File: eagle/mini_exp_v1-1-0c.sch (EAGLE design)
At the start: 34 parts, among them J1 CR22A-44D-2.54DS(70)STRAIGHT, J2 CR22A-44D-2.54DS(70)STRAIGHT, J3 DB9-MALE-RA, J4 DB9-MALE-RA, Q1 2N3904, U1 AY-3-8910, U2 74LS244N, U3 74LS244N, U4 74LS74N, U5 74LS30N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

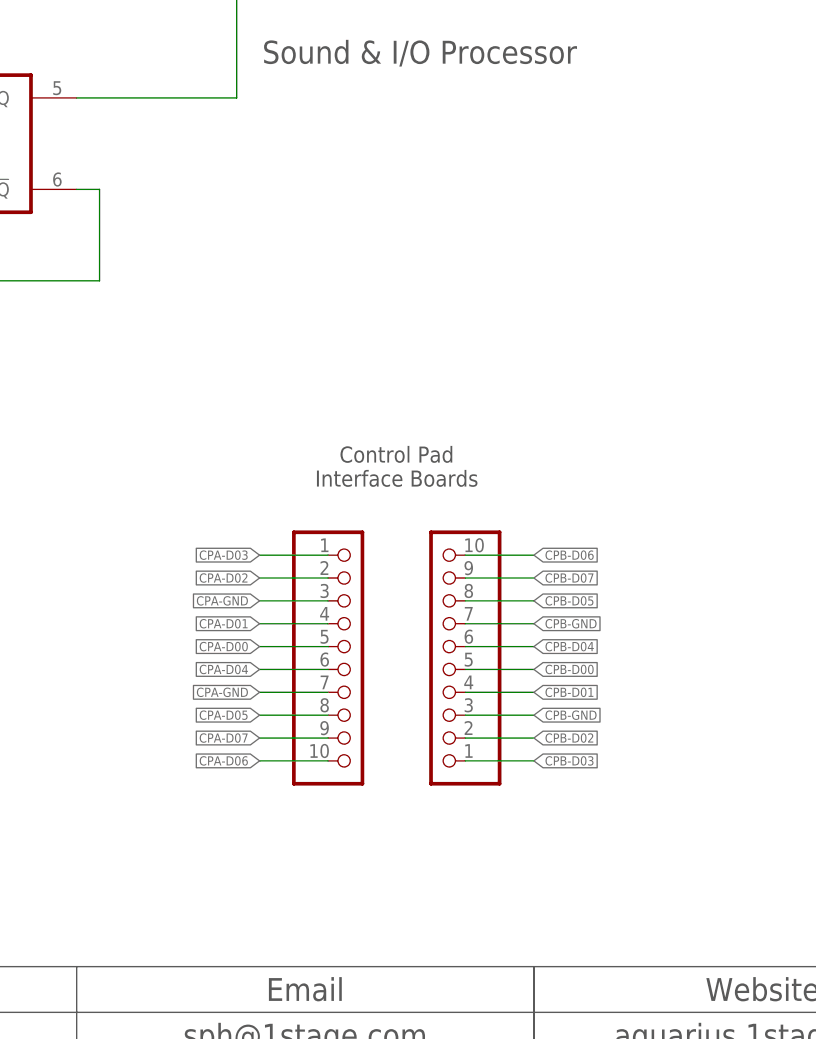
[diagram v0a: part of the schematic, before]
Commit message: Added IO Header to Rev C
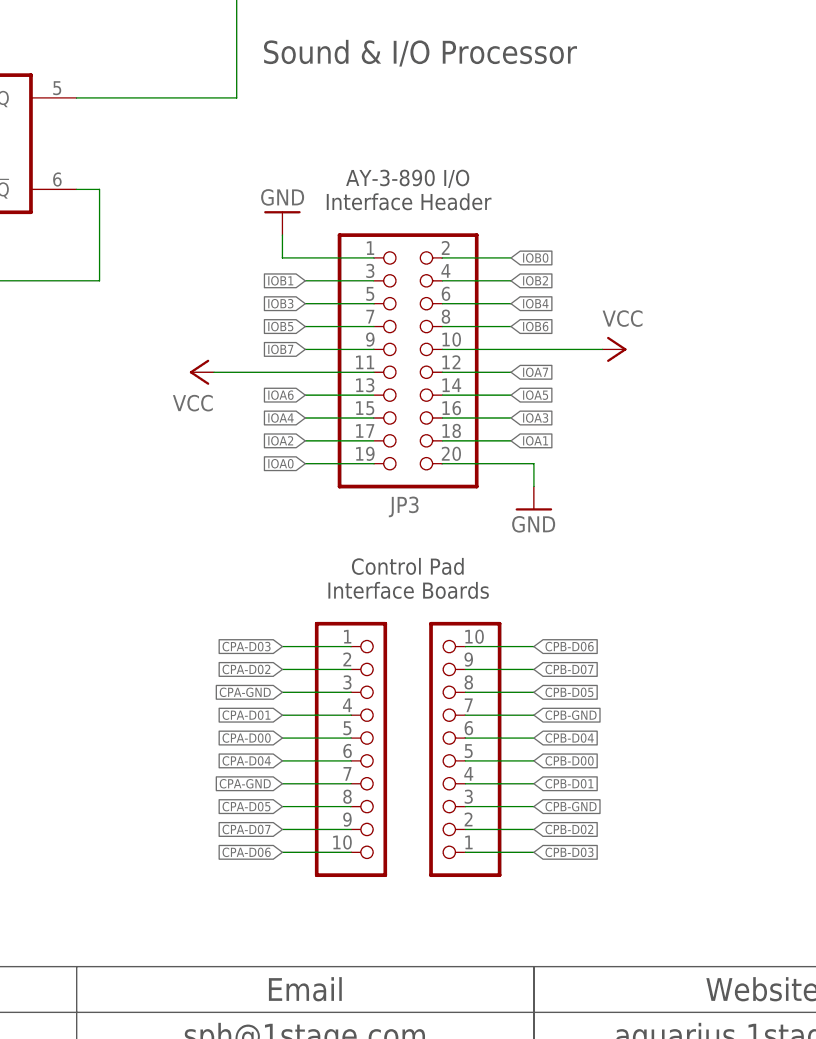
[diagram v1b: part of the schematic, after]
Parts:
- added JP3: (no value), aquarius2:PINHD-2X10
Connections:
- removed net N$100: J4.P$3, U1.IOB6
- removed net N$101: J4.P$9, U1.IOB3
- removed net N$102: J3.P$2, U1.IOA7
- removed net N$103: J3.P$3, U1.IOA6
- removed net N$104: J3.P$4, U1.IOA5
- removed net N$105: J3.P$5, U1.IOA4
- removed net N$106: J3.P$6, U1.IOA0
- removed net N$107: J3.P$7, U1.IOA1
- removed net N$108: J3.P$8, U1.IOA2
- removed net N$109: J3.P$9, U1.IOA3
- removed net N$18: J4.P$6, U1.IOB0
- removed net N$94: J4.P$2, U1.IOB7
- removed net N$95: J4.P$7, U1.IOB1
- removed net N$96: J4.P$8, U1.IOB2
- removed net N$98: J4.P$5, U1.IOB4
- removed net N$99: J4.P$4, U1.IOB5
- new net IOA0: J3.P$6, JP3.19, U1.IOA0
- new net IOA1: J3.P$7, JP3.18, U1.IOA1
- new net IOA2: J3.P$8, JP3.17, U1.IOA2
- new net IOA3: J3.P$9, JP3.16, U1.IOA3
- new net IOA4: J3.P$5, JP3.15, U1.IOA4
- new net IOA5: J3.P$4, JP3.14, U1.IOA5
- new net IOA6: J3.P$3, JP3.13, U1.IOA6
- new net IOA7: J3.P$2, JP3.12, U1.IOA7
- new net IOB0: J4.P$6, JP3.2, U1.IOB0
- new net IOB1: J4.P$7, JP3.3, U1.IOB1
- new net IOB2: J4.P$8, JP3.4, U1.IOB2
- new net IOB3: J4.P$9, JP3.5, U1.IOB3
- new net IOB4: J4.P$5, JP3.6, U1.IOB4
- new net IOB5: J4.P$4, JP3.7, U1.IOB5
- new net IOB6: J4.P$3, JP3.8, U1.IOB6
- new net IOB7: J4.P$2, JP3.9, U1.IOB7
- net GND: now also JP3.1, JP3.20
- net VCC: now also JP3.10, JP3.11
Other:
- note added: "AY-3-890 I/O Interface Header"
